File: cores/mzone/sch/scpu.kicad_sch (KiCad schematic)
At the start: 33 parts, among them X1 14.318MHZ

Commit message: mzone core sch
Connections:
- net DB0: now also B8.37 (DA0)
- net DB1: now also B8.36 (DA1)
- net DB2: now also B8.35 (DA2)
- net DB3: now also B8.34 (DA3)
- net DB4: now also B8.33 (DA4)
- net DB5: now also B8.32 (DA5)
- net DB6: now also B8.31 (DA6)
- net DB7: now also B8.30 (DA7)
- net GND: now also B8.1 (VSS), B8.24 (~{A9})
- net VCC: now also B8.25 (A8), B8.28 (BC2), B8.40 (VCC)
- net CK1M79: now reaches B8.22 (CLK)
- net CK1M79: now also A11.12, R53.2
- no-connect marks 6 -> 11

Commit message: mzone core sch
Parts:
- added unit 5 of A11
- added unit 4 of A11
- added AR6: R_Network04, Resistor_THT:R_Array_SIP5, symbol Device:R_Network04
- added B_B12, B_DE12, B_DE9: 74LS32, symbol jt74:74LS32
- added B_B7: 74LS138, symbol jt74:74LS138
- added B_C11: 74LS08, symbol jt74:74LS08
- added B_C9: 74LS74, symbol jt74:74LS74
- added B_DE11: 74LS02, symbol jt74:74LS02
- added B_RA8: 4.7k x 4, Resistor_THT:R_Array_SIP5, symbol Device:R_Network04
- added DE6: 27C64, symbol jt_rom:27C64
- added U?: Z80, symbol jt_cpu:Z80
- renumbered A12 to B_A12, A2 to B_A2, A3 to B_A3, B10 to B_B10, B11 to B_B11, B4 to B_B4, B8 to B_B8, B9 to B_B9, D4 to B_D4, E4 to B_E4, F4 to B_F4, G4 to B_G4
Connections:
- net AS0: now also A11.9, B_B12.4, B_DE11.11, DE6.10 (A0)
- net AS1: now also B_DE11.2, DE6.9 (A1)
- net DB0: now also DE6.11 (D0), U?.14 (D0)
- net DB1: now also DE6.12 (D1), U?.15 (D1)
- net DB2: now also DE6.13 (D2), U?.12 (D2)
- net DB3: now also DE6.15 (D3), U?.8 (D3)
- net DB4: now also DE6.16 (D4), U?.7 (D4)
- net DB5: now also DE6.17 (D5), U?.9 (D5)
- net DB6: now also DE6.18 (D6), U?.10 (D6)
- net DB7: now also DE6.19 (D7), U?.13 (D7)
- net GND: now also DE6.14 (GND), DE6.22 (~{OE}), U?.29 (GND)
- net VCC: now also AR6.1 (common), B_C9.1 (~{R}), B_C9.10 (~{S}), B_C9.12 (D), B_C9.2 (D), B_RA8.1 (common), DE6.1 (VPP), DE6.26 (NC), DE6.27 (~{PGM}), DE6.28 (VCC), U?.11 (VCC)
- net YA4: now also B_B9.11 (CKB), B_B9.9 (Q0), B_RA8.2 (R1)
- net YA5: now also B_B9.5 (Q1), B_RA8.4 (R3)
- net YA6: now also B_B9.4 (Q2), B_RA8.5 (R4)
- net YA7: now also B_B9.8 (Q3), B_RA8.3 (R2)
- net ~{CABINP}: now also B_B7.12 (O3)
- net ~{CODE}: now also B_B7.13 (O2)
- net ~{RESET}: now also B_C11.12, B_C11.9, U?.26 (~{RESET})
- net ~{START}: now also B_B7.14 (O1)
- new net: B_C11.11, B_C9.13 (~{R})
- new net: B_C11.13, B_DE9.8
- new net: A11.10, B_DE12.1
- new net: B_B12.6, B_C11.10
- new net: B_C11.8, B_C9.4 (~{S})
- new net: A11.8, B_B12.9
- new net: B_DE11.12, B_DE11.3, B_DE12.3
- new net AS0': U?.30 (A0)
- new net AS1': U?.31 (A1)
- new net AS10: DE6.21 (A10), U?.40 (A10)
- new net AS11: DE6.23 (A11), U?.1 (A11)
- new net AS12: DE6.2 (A12), U?.2 (A12)
- new net AS13: B_B7.1 (A0), U?.3 (A13)
- new net AS14: B_B7.2 (A1), U?.4 (A14)
- new net AS15: B_B7.3 (A2), U?.5 (A15)
- new net AS2: DE6.8 (A2), U?.32 (A2)
- new net AS3: DE6.7 (A3), U?.33 (A3)
- new net AS4: DE6.6 (A4), U?.34 (A4)
- new net AS5: DE6.5 (A5), U?.35 (A5)
- new net AS6: DE6.4 (A6), U?.36 (A6)
- new net AS7: DE6.3 (A7), U?.37 (A7)
- new net AS8: DE6.25 (A8), U?.38 (A8)
- new net AS9: DE6.24 (A9), U?.39 (A9)
- new net BLANK: B_C9.11 (C)
- new net CPUCLK: U?.6 (~{CLK})
- new net INTSND: B_C9.3 (C)
- new net ~{AFR2}: B_B12.8
- new net ~{AYBC2}: B_DE11.1
- new net ~{AYDIR}: B_DE11.13
- new net ~{DIP}: B_B7.11 (O4)
- new net ~{INTMAIN}: B_B7.10 (O5)
- new net ~{SBUS}: AR6.3 (R2), U?.25 (~{BUSRQ})
- new net ~{SINT}: AR6.2 (R1), B_C9.8 (~{Q}), U?.16 (~{INT})
- new net ~{SIORQ}: B_DE12.2, B_DE9.10, U?.20 (~{IORQ})
- new net ~{SM1}: A11.11, B_DE9.9, U?.27 (~{M1})
- new net ~{SMREQ}: B_B7.4 (E1), B_B7.5 (E2), U?.19 (~{MREQ})
- new net ~{SNMI}: AR6.4 (R3), B_C9.5 (Q), U?.17 (~{NMI})
- new net ~{SRD}: U?.21 (~{RD})
- new net ~{SRFSH}: B_B7.6 (E3), U?.28 (~{RFSH})
- new net ~{SROM}: B_B7.15 (O0)
- new net ~{SVRAM}: B_B7.7 (O7)
- new net ~{WAIT}: AR6.5 (R4), U?.24 (~{WAIT})
- new net ~{WDOG}: B_B12.5, B_B7.9 (O6)
- no-connect marks 11 -> 15
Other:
- note added: "DIV4096"
- note added: "KONAMI-1: MA, MB Z80: SA, DB I8039: IA, IB"
- note added: "YA4 14.318MHz/8192 = 1747.8Hz YA5 14.318MHz/16384 = 873.9Hz YA6 14.318MHz/32768 = 437.0Hz YA7 14.318MHz/65536 = 218.5Hz"
- note added: "gör dessa till B_D14"
- moved on the sheet: B_A12B, D14D, D14E, D14F, D14G, D14H, D14I

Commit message: mzone core
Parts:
- removed B_E4, B_F4, B_G4: 74LS253, symbol jt74:74LS253
- removed C? (x8): 100nF, symbol Device:C
- removed RA3: 22k x 8, Resistor_THT:R_Array_SIP9, symbol Device:R_Network08_Split
- removed U?: 74LS293, symbol jt74:74LS293
- removed U?: KONAMI_EDGE, symbol konami:KONAMI_EDGE
- added A6, B_A5: 4066, symbol 4xxx:4066
- added B_B1, B_B6: LM324, symbol Amplifier_Operational:LM324
- added B_C1, B_C29, B_C30, B_C33, B_C6, B_C7, B_C8: 10n, symbol Device:C
- added B_C28, B_C31, B_C32: 220n, symbol Device:C_Polarized
- added B_C3: LA4460, symbol skutis:LA4460
- added B_C5, C4: 100u, symbol Device:C_Polarized
- added B_R1, B_R2: 4R7, symbol Device:R
- added B_R24, B_R25, B_R26, B_R27, B_R28, B_R29, B_R30, B_R31, B_R39: 200k, symbol Device:R
- added B_R32, B_R33, B_R34, B_R35, B_R36, B_R37, B_R38: 100k, symbol Device:R
- added B_R48: 4k7, symbol Device:R
- added B_R49, B_R50: 470R, symbol Device:R
- added B_VR200: 180R, symbol Device:R_Potentiometer
- added C9: 1000u, symbol Device:C_Polarized
- added R40, R41, R42: 1k, symbol Device:R
- added R43, R44, R45, R46: 10k, symbol Device:R
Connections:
- net ~{AYBC2} is gone; now on net ~{AYBC1}: B_DE11.1
- net GND: now also B_B4.1 (T0), D14.19, B_C1.2, B_C28.2, B_C29.2, B_C3.3 (IN2+), B_C3.8 (GND), B_C30.2, B_C31.2, B_C32.2, B_C33.2, B_C8.2, B_R1.2, B_R2.2, B_R39.2, B_VR200.1, C4.2, C9.2
- net VCC: now also B_R48.1, B_R49.1, B_R50.1
- net ~{AYDIR}: now also B_B8.27 (BDIR)
- net at D14.12: now also B_B4.2 (X1), D14.11, B_R49.2
- net CK7M16: now reaches D14.8
- net CK7M16: now also B_A12.11 (CKB), B_A12.9 (Q0)
- net CHB1: now reaches B_B8.10 (IOB3)
- net CHB1: now also A6.6
- net CHB0: now reaches B_B8.11 (IOB2)
- net CHB0: now also A6.5
- net CHA1: now reaches B_B8.12 (IOB1)
- net CHA1: now also A6.13
- net CHA0: now reaches B_B8.13 (IOB0)
- net CHA0: now also A6.12
- net ~{AYBC1}: now reaches B_B8.29 (BC1)
- net at B_B8.3 (CHB): now also R41.1
- net at B_B8.38 (CHC): now also R40.1
- net at B_B8.4 (CHA): now also R42.1
- net CHC1: now reaches B_B8.8 (IOB5)
- net CHC1: now also B_A5.6
- net CHC0: now reaches B_B8.9 (IOB4)
- net CHC0: now also B_A5.12
- net DAC0: now reaches B_B4.27 (P10)
- net DAC0: now also B_R31.1
- net DAC1: now reaches B_B4.28 (P11)
- net DAC1: now also B_R30.1
- net DAC2: now reaches B_B4.29 (P12)
- net DAC2: now also B_R29.1
- net at B_B4.3 (X2): now also D14.9, B_R50.2
- net DAC3: now reaches B_B4.30 (P13)
- net DAC3: now also B_R28.1
- net DAC4: now reaches B_B4.31 (P14)
- net DAC4: now also B_R27.1
- net DAC5: now reaches B_B4.32 (P15)
- net DAC5: now also B_R26.1
- net DAC6: now reaches B_B4.33 (P16)
- net DAC6: now also B_R25.1
- net DAC7: now reaches B_B4.34 (P17)
- net DAC7: now also B_R24.1
- net at B_B4.5 (~{SS}): now also B_B4.7 (EA), B_R48.2
- new net: B_R25.2, B_R32.2, B_R33.1
- new net: B_R26.2, B_R33.2, B_R34.1
- new net: B_A5.10, B_C29.1
- new net: B_C7.2, B_R1.1
- new net: B_A5.11, B_A5.9, R40.2, R45.1
- new net: A6.4, A6.8, R41.2, R44.1
- new net: B_B6.3 (+), B_R24.2, B_R32.1
- new net: B_A5.8, B_C28.1
- new net: B_B6.1, B_B6.2 (-), R46.1
- new net: B_VR200.3, R43.2, R44.2, R45.2, R46.2
- new net: B_R30.2, B_R37.2, B_R38.1
- new net: B_C3.2 (IN1+), B_C8.1, B_VR200.2
- new net: B_C3.6 (DC), C4.1
- new net: A6.1, A6.11, R42.2, R43.1
- new net: B_R31.2, B_R38.2, B_R39.1
- new net: B_R29.2, B_R36.2, B_R37.1
- new net: B_R28.2, B_R35.2, B_R36.1
- new net: A6.9, B_C32.1
- new net: A6.3, B_C30.1
- new net: B_R27.2, B_R34.2, B_R35.1
- new net: A6.10, B_C33.1
- new net: B_C1.1, B_C3.5 (IN2-), B_C5.2
- new net: B_C6.2, B_R2.1
- new net: A6.2, B_C31.1
- new net: B_C3.4 (IN1-), B_C5.1
- new net +12V: B_C3.10 (VCC), C9.1
- new net SPK+: B_C3.7 (OUT2), B_C7.1
- new net SPK-: B_C3.9 (OUT1), B_C6.1
- no-connect marks 15 -> 16
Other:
- moved on the sheet: A11A, A11B, A11C, A11D, A11E, A11F, AR6, B_A12A, B_A2, B_A3, B_B10A, B_B11A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

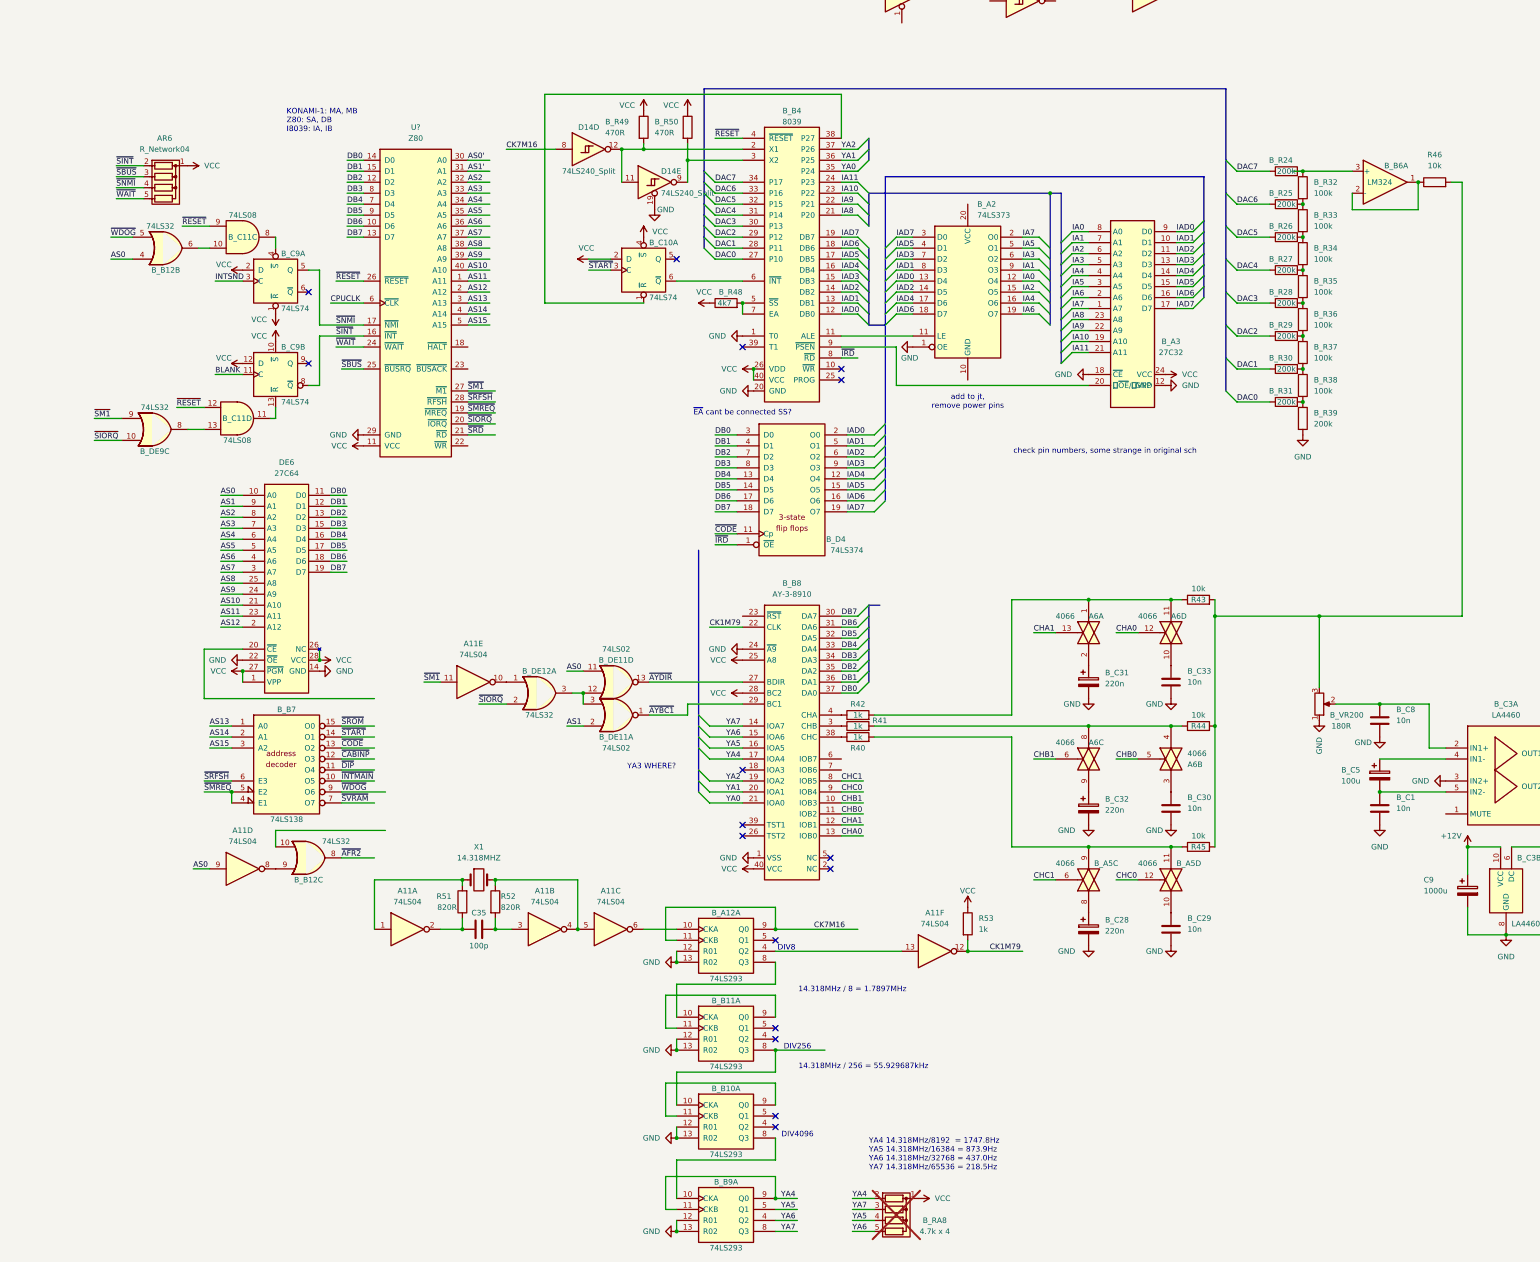
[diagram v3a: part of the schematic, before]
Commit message: mzone core
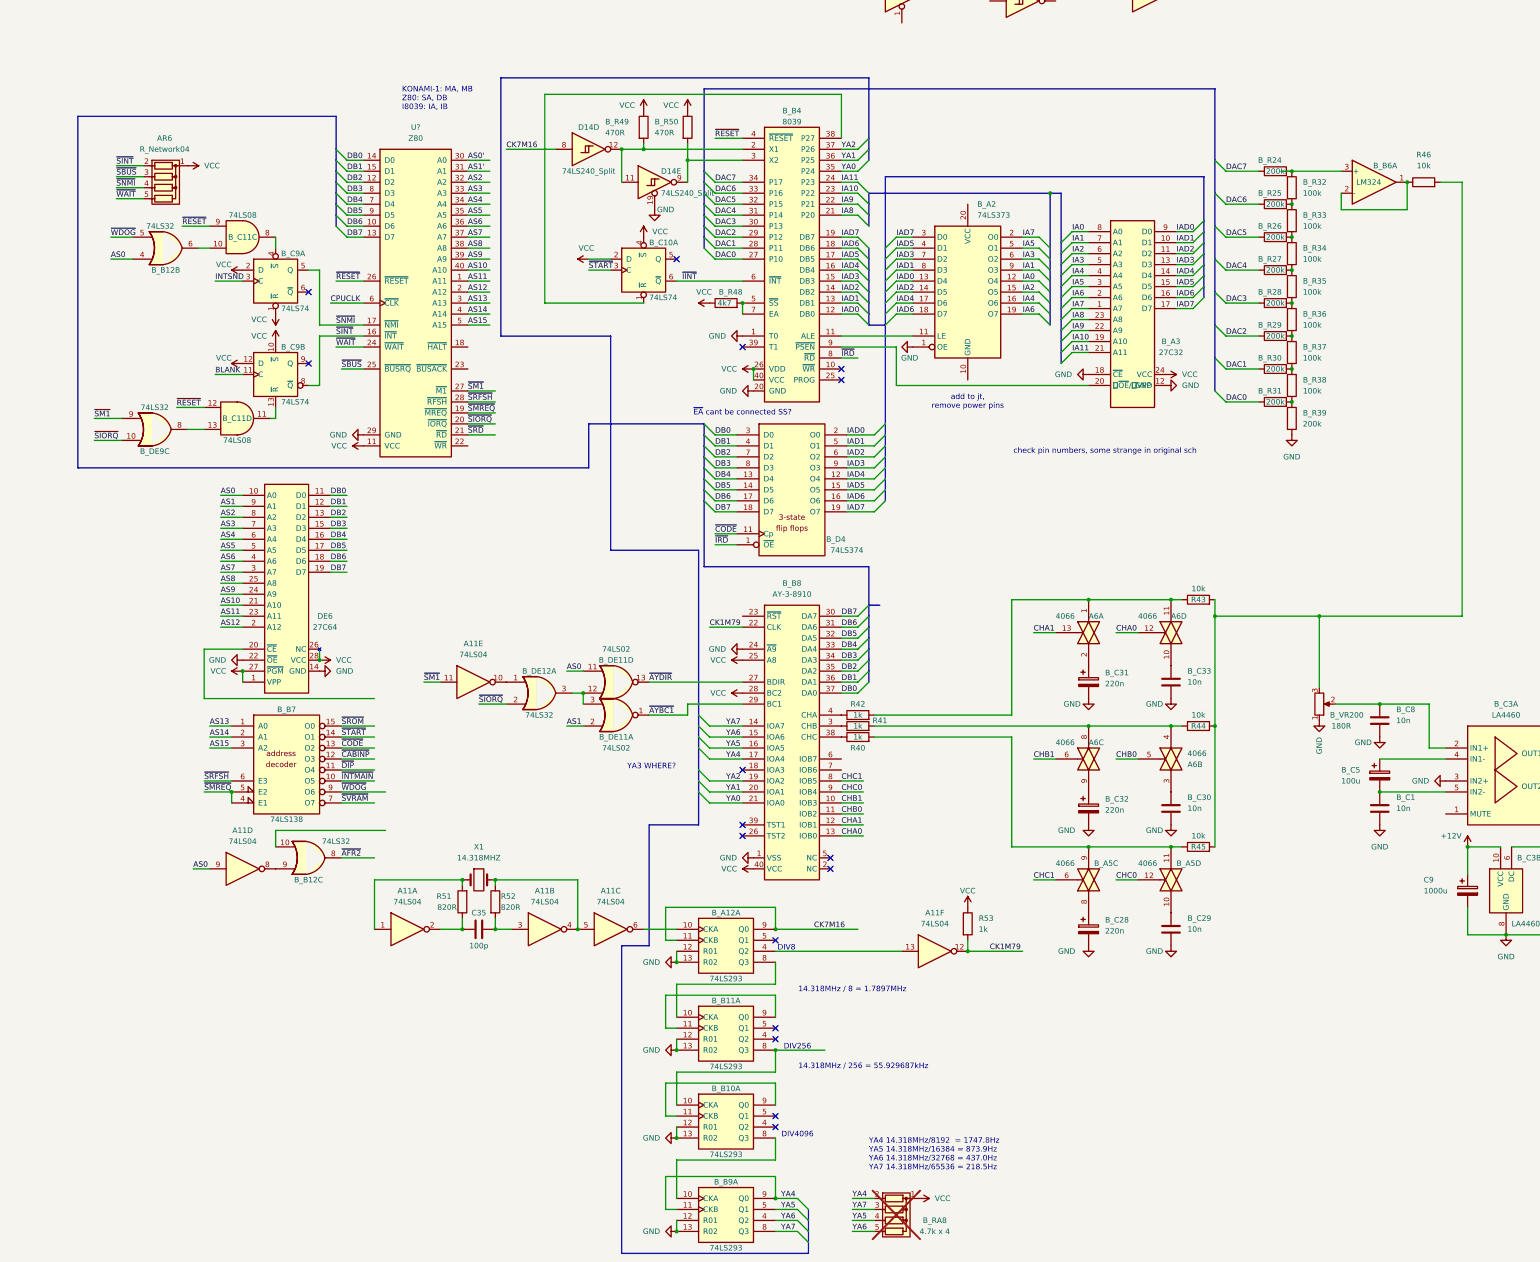
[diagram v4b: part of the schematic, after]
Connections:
- net ~{IINT}: now reaches B_B4.6 (~{INT}), B_C10.6 (~{Q})
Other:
- moved on the sheet: B_B6A, B_R24, B_R25, B_R26, B_R27, B_R28, B_R29, B_R30, B_R31, B_R32, B_R33, B_R34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

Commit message: mzone core
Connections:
- net ~{WDOG}: now also B_B12.10
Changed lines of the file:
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@@
 		)
 	)
+	(wire
+		(pts
+			(xy 96.52 176.53) (xy 96.52 185.42)
+		)
+		(stroke
+			(width 0)
+			(type default)
+		)
+	)
 	(bus
 		(pts
@@
 	(wire
 		(pts
-			(xy 86.36 191.77) (xy 93.98 191.77)
-		)
-		(stroke
-			(width 0)
-			(type default)
-		)
-	)
-	(wire
-		(pts
 			(xy 241.3 132.08) (xy 241.3 158.75)
 		)
@@
 		)
 	)
-	(label "~{AFR2}"
-		(at 86.36 191.77 0)
-		(fields_autoplaced yes)
-		(effects
-			(font
-				(size 1.27 1.27)
-			)
-			(justify left bottom)
-		)
-	)
 	(label "YA7"
 		(at 204.47 273.05 0)
@@
 		)
 	)
+	(hierarchical_label "~{AFR2}"
+		(shape output)
+		(at 86.36 191.77 0)
+		(fields_autoplaced yes)
+		(effects
+			(font
+				(size 1.27 1.27)
+			)
+			(justify left)
+		)
+	)
